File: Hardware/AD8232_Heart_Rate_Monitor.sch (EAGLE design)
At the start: 33 parts, among them U1 AD8232

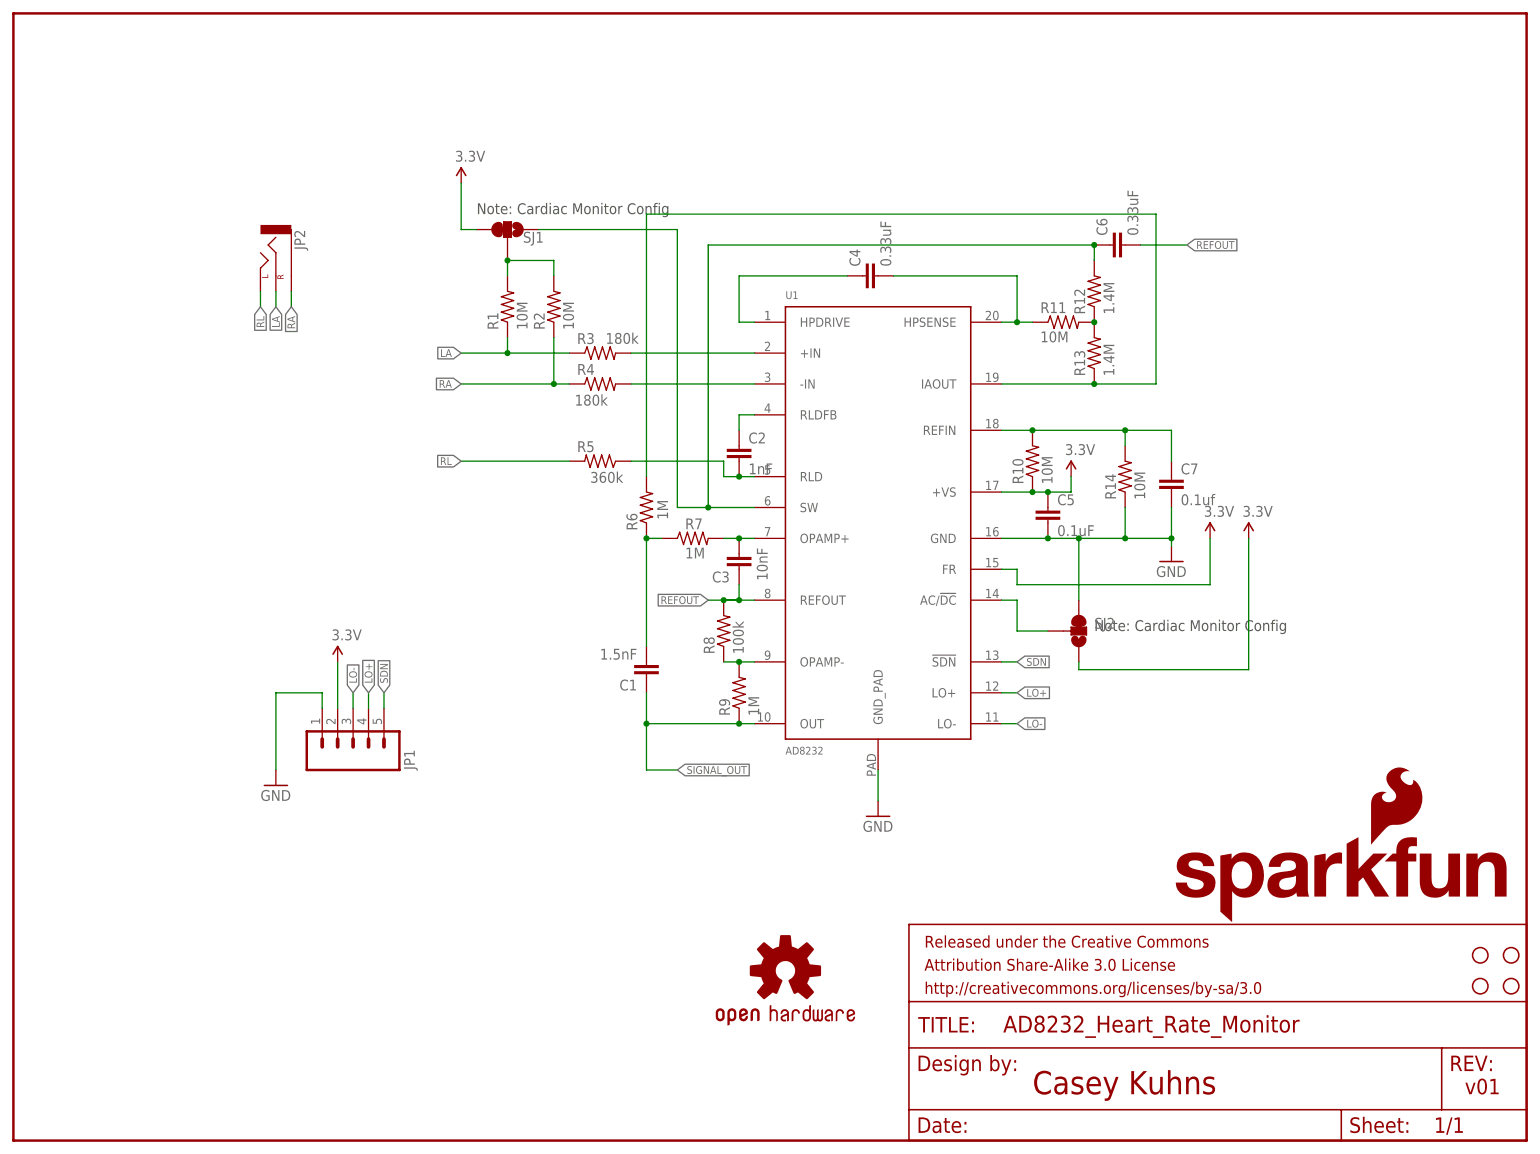
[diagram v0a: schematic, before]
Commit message: Changes made
1. Added signal output pin
2. Added pull-up resistor on shutdown pin to keep chip active by default.
3. Moved some labels around to let everything fit
4. fixed exposed vias.
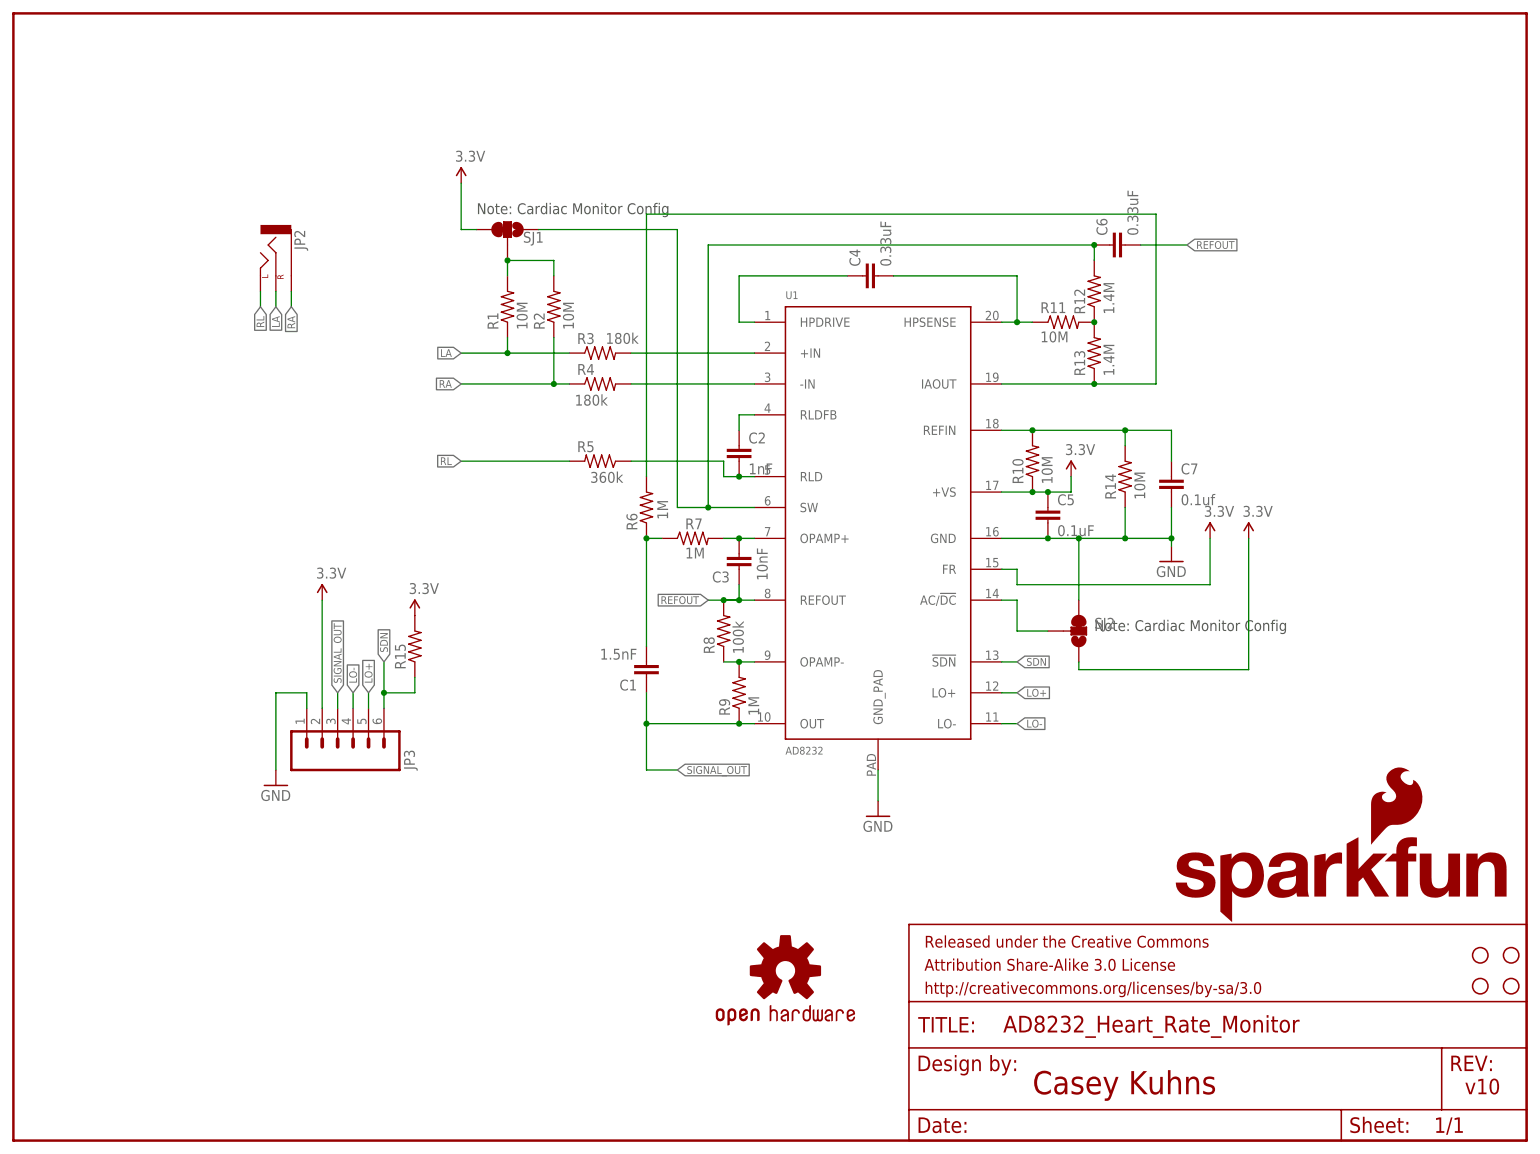
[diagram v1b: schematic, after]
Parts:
- removed JP1: (no value), SparkFun-Connectors:M05PTH
- added JP3: (no value), SparkFun-Connectors:M06SIP
- added R15: (no value), SparkFun-Resistors:10KOHM1/10W1%(0603)0603
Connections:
- net 3.3V: now also JP3.2, R15.2; no longer JP1.2
- net GND: now also JP3.1; no longer JP1.1
- net LO+: now also JP3.5; no longer JP1.4
- net LO-: now also JP3.4; no longer JP1.3
- net SDN: now also JP3.6, R15.1; no longer JP1.5
- net SIGNAL_OUT: now also JP3.3
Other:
- note added: "v10"
- note removed: "v01"
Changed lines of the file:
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@@
 <?xml version="1.0" encoding="utf-8"?>
 <!DOCTYPE eagle SYSTEM "eagle.dtd">
-<eagle version="6.5.0">
+<eagle version="6.0">
 <drawing>
 <settings>
@@
 <part name="SUPPLY4" library="SparkFun-Aesthetics" deviceset="3.3V" device=""/>
 <part name="JP2" library="SparkFun-Connectors" deviceset="AUDIO-JACK" device="SMD2"/>
-<part name="JP1" library="SparkFun-Connectors" deviceset="M05" device="PTH"/>
 <part name="GND3" library="SparkFun-Aesthetics" deviceset="GND" device=""/>
 <part name="SUPPLY5" library="SparkFun-Aesthetics" deviceset="3.3V" device=""/>
@@
 <part name="LOGO2" library="SparkFun-Aesthetics" deviceset="SFE_LOGO_NAME_FLAME" device=".1_INCH"/>
 <part name="LOGO1" library="SparkFun-Aesthetics" deviceset="OSHW-LOGO" device="S"/>
+<part name="JP3" library="SparkFun-Connectors" deviceset="M06" device="SIP"/>
+<part name="R15" library="SparkFun-Resistors" deviceset="10KOHM1/10W1%(0603)" device="0603"/>
+<part name="SUPPLY6" library="SparkFun-Aesthetics" deviceset="3.3V" device=""/>
 </parts>
 <sheets>
@@
 <plain>
 <text x="167.64" y="7.62" size="3.81" layer="94" font="vector">Casey Kuhns</text>
-<text x="238.76" y="7.62" size="2.54" layer="94" font="vector">v01</text>
+<text x="238.76" y="7.62" size="2.54" layer="94" font="vector">v10</text>
 <text x="76.2" y="152.4" size="1.778" layer="97">Note: Cardiac Monitor Config</text>
 <text x="177.8" y="83.82" size="1.778" layer="97">Note: Cardiac Monitor Config</text>
@@
 <instance part="SUPPLY4" gate="G$1" x="203.2" y="99.06"/>
 <instance part="JP2" gate="G$1" x="43.18" y="144.78" rot="R270"/>
-<instance part="JP1" gate="G$1" x="55.88" y="63.5" rot="MR90"/>
 <instance part="GND3" gate="1" x="43.18" y="58.42"/>
-<instance part="SUPPLY5" gate="G$1" x="53.34" y="78.74"/>
+<instance part="SUPPLY5" gate="G$1" x="50.8" y="88.9"/>
 <instance part="STANDOFF4" gate="G$1" x="246.38" y="25.4"/>
 <instance part="STANDOFF3" gate="G$1" x="246.38" y="30.48"/>
@@
 <instance part="LOGO2" gate="G$1" x="190.5" y="35.56"/>
 <instance part="LOGO1" gate="G$1" x="127" y="27.94"/>
+<instance part="JP3" gate="G$1" x="53.34" y="66.04" rot="MR90"/>
+<instance part="R15" gate="G$1" x="66.04" y="81.28" rot="R90"/>
+<instance part="SUPPLY6" gate="G$1" x="66.04" y="86.36"/>
 </instances>
 <busses>
@@
 </segment>
 <segment>
-<pinref part="JP1" gate="G$1" pin="1"/>
 <pinref part="GND3" gate="1" pin="GND"/>
 <wire x1="43.18" y1="60.96" x2="43.18" y2="73.66" width="0.1524" layer="91"/>
-<wire x1="43.18" y1="73.66" x2="50.8" y2="73.66" width="0.1524" layer="91"/>
-<wire x1="50.8" y1="73.66" x2="50.8" y2="71.12" width="0.1524" layer="91"/>
+<wire x1="43.18" y1="73.66" x2="48.26" y2="73.66" width="0.1524" layer="91"/>
+<pinref part="JP3" gate="G$1" pin="1"/>
+<wire x1="48.26" y1="71.12" x2="48.26" y2="73.66" width="0.1524" layer="91"/>
 </segment>
 </net>
@@
 <label x="109.22" y="60.96" size="1.27" layer="95" xref="yes"/>
 <junction x="104.14" y="68.58"/>
+</segment>
+<segment>
+<pinref part="JP3" gate="G$1" pin="3"/>
+<wire x1="53.34" y1="71.12" x2="53.34" y2="73.66" width="0.1524" layer="91"/>
+<label x="53.34" y="73.66" size="1.27" layer="95" rot="R90" xref="yes"/>
 </segment>
 </net>
@@
 </segment>
 <segment>
-<pinref part="JP1" gate="G$1" pin="2"/>
+<pinref part="JP3" gate="G$1" pin="2"/>
 <pinref part="SUPPLY5" gate="G$1" pin="3.3V"/>
-<wire x1="53.34" y1="71.12" x2="53.34" y2="78.74" width="0.1524" layer="91"/>
+<wire x1="50.8" y1="88.9" x2="50.8" y2="71.12" width="0.1524" layer="91"/>
+</segment>
+<segment>
+<pinref part="R15" gate="G$1" pin="2"/>
+<pinref part="SUPPLY6" gate="G$1" pin="3.3V"/>
 </segment>
 </net>
@@
 </segment>
 <segment>
-<pinref part="JP1" gate="G$1" pin="4"/>
 <wire x1="58.42" y1="71.12" x2="58.42" y2="73.66" width="0.1524" layer="91"/>
 <label x="58.42" y="73.66" size="1.27" layer="95" rot="R90" xref="yes"/>
+<pinref part="JP3" gate="G$1" pin="5"/>
 </segment>
 </net>
@@
 </segment>
 <segment>
-<pinref part="JP1" gate="G$1" pin="3"/>
 <wire x1="55.88" y1="71.12" x2="55.88" y2="73.66" width="0.1524" layer="91"/>
 <label x="55.88" y="73.66" size="1.27" layer="95" rot="R90" xref="yes"/>
+<pinref part="JP3" gate="G$1" pin="4"/>
 </segment>
 </net>
@@
 <net name="SDN" class="0">
 <segment>
-<pinref part="JP1" gate="G$1" pin="5"/>
 <wire x1="60.96" y1="71.12" x2="60.96" y2="73.66" width="0.1524" layer="91"/>
-<label x="60.96" y="73.66" size="1.27" layer="95" rot="R90" xref="yes"/>
-</segment>
-<segment>
+<label x="60.96" y="78.74" size="1.27" layer="95" rot="R90" xref="yes"/>
+<pinref part="JP3" gate="G$1" pin="6"/>
+<wire x1="60.96" y1="73.66" x2="60.96" y2="78.74" width="0.1524" layer="91"/>
+<wire x1="60.96" y1="73.66" x2="66.04" y2="73.66" width="0.1524" layer="91"/>
+<wire x1="66.04" y1="73.66" x2="66.04" y2="76.2" width="0.1524" layer="91"/>
+<pinref part="R15" gate="G$1" pin="1"/>
+<junction x="60.96" y="73.66"/>
+</segment>
+<segment>
